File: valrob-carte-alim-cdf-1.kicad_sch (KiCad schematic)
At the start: 31 parts, among them J1 USB_C_Receptacle_USB2.0_14P, J26 Conn_01x02, J6 Conn_01x04_Pin, SW1 SW_Push, SW2 SW_Push, SW3 SW_Push, U3 SN65HVD230, U4 ESP32-S3-WROOM-1

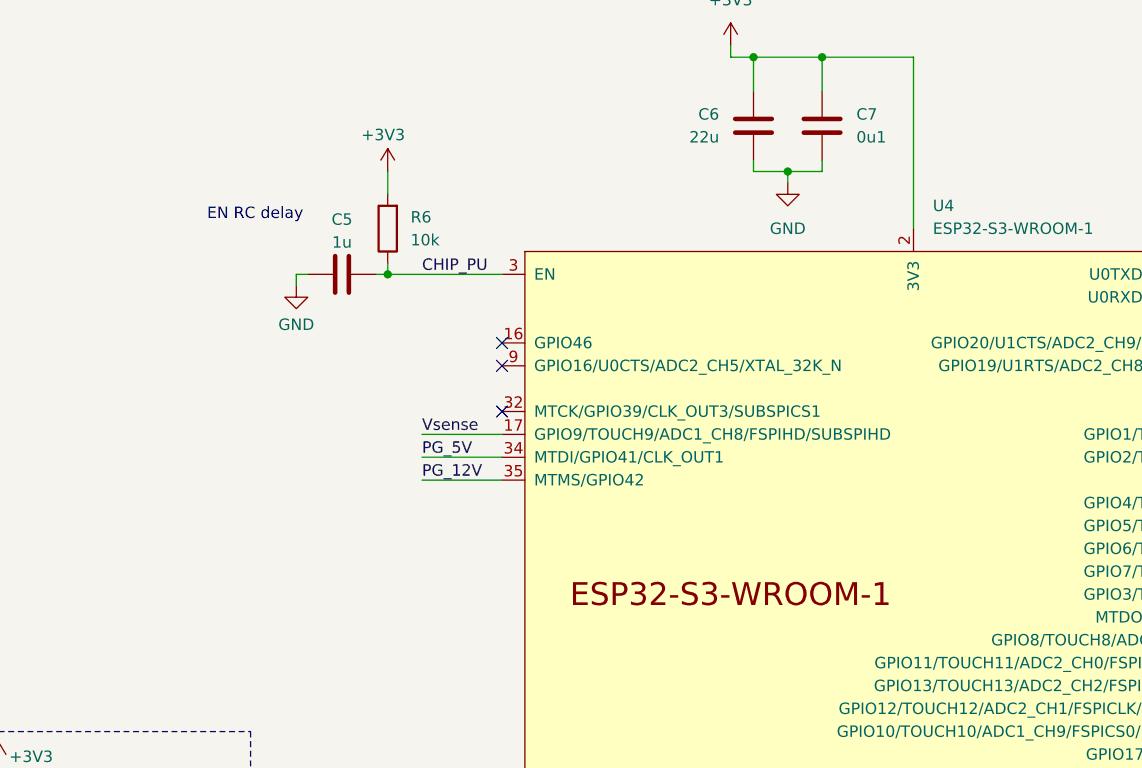
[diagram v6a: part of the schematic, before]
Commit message: schem: add general power status leds
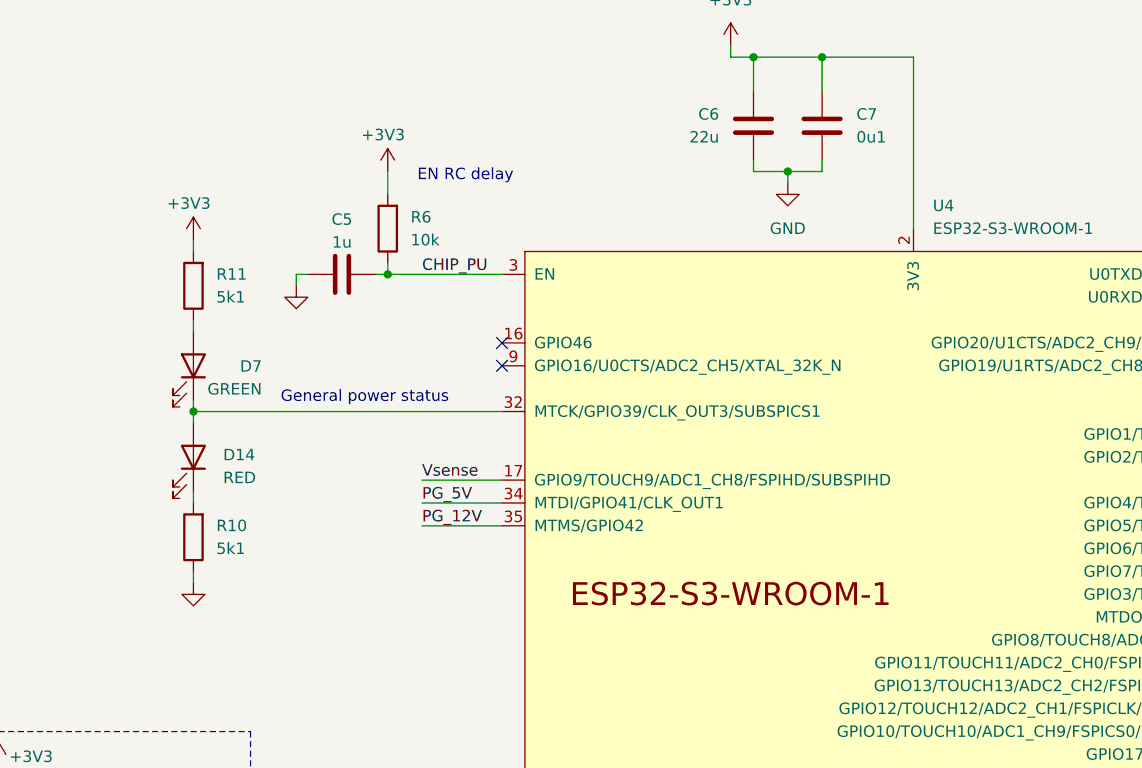
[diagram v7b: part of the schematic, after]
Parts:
- added D14: RED, LED_SMD:LED_0603_1608Metric, symbol Device:LED
- added D7: GREEN, LED_SMD:LED_0805_2012Metric, symbol Device:LED
- added R10, R11: 5k1, Resistor_SMD:R_0402_1005Metric, symbol Device:R
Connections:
- net +3V3: now also R11.2
- net GND: now also R10.1
- net at U4.32 (MTCK/GPIO39/CLK_OUT3/SUBSPICS1): now also D14.2 (A), D7.1 (K)
- new net: D14.1 (K), R10.2
- new net: D7.2 (A), R11.1
- no-connect marks 5 -> 4
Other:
- note added: "General power status"

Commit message: schem: run and fix ERC
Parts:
- removed D16, D17, D18: H5VU10U, Pers:Diode_DFN1006, symbol Pers:H5VU10U
- added D16, D17, D18: H5VU10U, GLCS:Diode_DFN1006, symbol GLCS:H5VU10U
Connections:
- net D+: now also D18.1 (K)
- net D-: now also D16.1 (K)
- net GND: now also D16.2 (A), D17.2 (A), D18.2 (A)
- net VBUS: now also D17.1 (K)
- net EN_12V_4: no longer names the net of U4.22 (GPIO14/TOUCH14/ADC2_CH3/FSPIWP/FSPIDQS/SUBSPIWP)
- no-connect marks 4 -> 5
